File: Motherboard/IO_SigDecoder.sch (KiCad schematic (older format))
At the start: 8 parts, among them U30 74LS04, U34 74LS04, U35 74LS04, U36 74LS00, U37 74LS00, U38 74LS10

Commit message: Large sync
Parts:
- added R11: 6k2, Resistors_THT:R_Axial_DIN0204_L3.6mm_D1.6mm_P7.62mm_Horizontal, symbol Device:R
- added SW5: SW_DIP_x01, Housings_DIP:DIP-4_W7.62mm, symbol Switch:SW_DIP_x01
- added U50: 74LS04, Housings_DIP:DIP-14_W7.62mm_Socket, symbol 74xx:74LS04
- added U51: ATF750LVC, Housings_DIP:DIP-28_W7.62mm_Socket, symbol fdc:ATF750LVC
- added U52: 74LS74, Housings_DIP:DIP-14_W7.62mm_Socket, symbol 74xx:74LS74
- added U53: 74LS00, Housings_DIP:DIP-14_W7.62mm_Socket, symbol 74xx:74LS00
- added U54: 74LS08, Housings_DIP:DIP-14_W7.62mm_Socket, symbol 74xx:74LS08
- added U55: 74LS138, Housings_DIP:DIP-16_W7.62mm_Socket, symbol 74xx:74LS138
- added U56: 4077, Housings_DIP:DIP-14_W7.62mm_Socket, symbol 4xxx:4077
- added U57: DS1100Z-100+ (TTLDL-20), Housings_SOIC:SOIC-8_3.9x4.9mm_Pitch1.27mm, symbol DS1100Z-100+:DS1100Z-100+
- added U?: CD40147, MODULE, symbol CD40147:CD40147
- R10, R9: footprint (none) -> Resistors_THT:R_Axial_DIN0204_L3.6mm_D1.6mm_P7.62mm_Horizontal
- U30, U34, U35, U36, U37, U38: footprint (none) -> Housings_DIP:DIP-14_W7.62mm_Socket
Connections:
- net +5V: now also R11.2, U52.4 (~S), U55.16 (VCC)
- net at U38.12: now also U54.1
- new net: U53.3, U55.5 (E2)
- new net: R11.1, SW5.2, U53.2
- new net ALLOW_NMI: U52.5 (Q), U54.2
- new net GND: SW5.1, U55.8 (GND)
- new net NMI: U54.3
- new net RESET: U50.1
- new net ROMADDRSEL: U56.3
- new net XA15: U55.1 (A0)
- new net XA16: U55.2 (A1)
- new net XA17: U55.3 (A2)
- new net XA18: U53.1
- new net XA19: U55.6 (E3)
- new net XD7: U52.2 (D)
- new net ~CS6: U55.9 (O6), U56.1
- new net ~CS7: U55.7 (O7), U56.2
- new net ~RESET: U50.2, U52.1 (~R)
- new net ~WATNMIREG: U52.3 (C)
- new net ~XMEMR: U55.4 (E1)
- no-connect marks 0 -> 6
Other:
- note added: "Not used"
- note added: "U44 in techref"

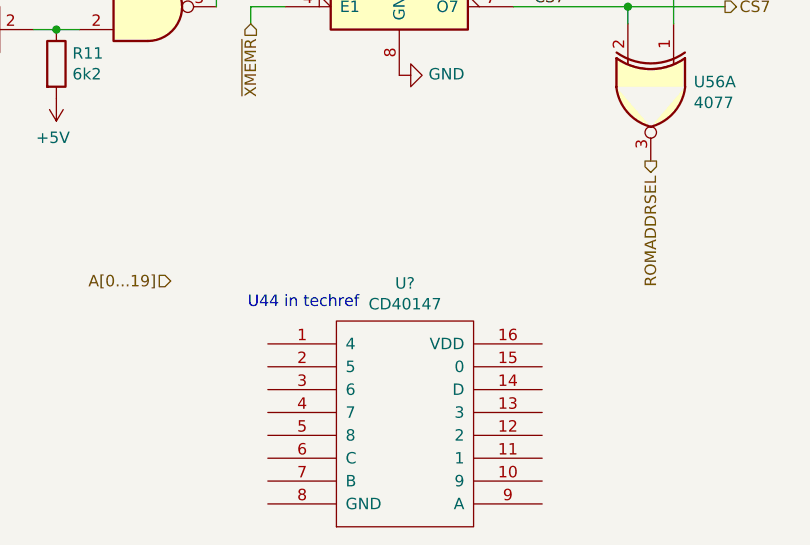
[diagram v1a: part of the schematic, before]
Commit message: Work on motherboard  - Integrating glue logic into CPLD  - Began work on routing
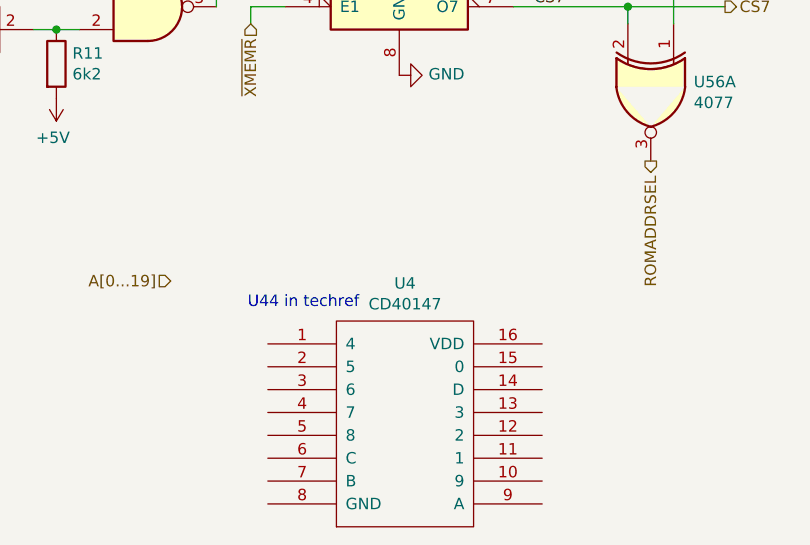
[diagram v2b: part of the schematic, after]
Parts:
- U4: renamed from U?; footprint MODULE -> Housings_DIP:DIP-16_W7.62mm_Socket
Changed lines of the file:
@@
 	1    0    0    -1
 $EndComp
-Wire Bus Line
-	6000 3725 6000 4125
 $Comp
-L CD40147:CD40147 U?
+L CD40147:CD40147 U4
 U 1 1 5CA70B41
 P 6775 6400
-F 0 "U?" H 6775 7015 50  0000 C CNN
+F 0 "U4" H 6775 7015 50  0000 C CNN
 F 1 "CD40147" H 6775 6924 50  0000 C CNN
-F 2 "MODULE" H 6775 6400 50  0001 C CNN
+F 2 "Housings_DIP:DIP-16_W7.62mm_Socket" H 6775 6400 50  0001 C CNN
 F 3 "DOCUMENTATION" H 6775 6400 50  0001 C CNN
 	1    6775 6400
@@
 Text Notes 6575 5900 2    50   ~ 0
 U44 in techref
+Wire Bus Line
+	6000 3725 6000 4125
 $EndSCHEMATC

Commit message: Large sync
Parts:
- removed R9: R, Resistors_THT:R_Axial_DIN0204_L3.6mm_D1.6mm_P7.62mm_Horizontal, symbol Device:R
- removed U35, U50: 74LS04, Housings_DIP:DIP-14_W7.62mm_Socket, symbol 74xx:74LS04
- removed unit 1 of U36
- removed unit 3 of U36
- removed U37, U53: 74LS00, Housings_DIP:DIP-14_W7.62mm_Socket, symbol 74xx:74LS00
- removed U38: 74LS10, Housings_DIP:DIP-14_W7.62mm_Socket, symbol 74xx:74LS10
- removed U52: 74LS74, Housings_DIP:DIP-14_W7.62mm_Socket, symbol 74xx:74LS74
- removed U54: 74LS08, Housings_DIP:DIP-14_W7.62mm_Socket, symbol 74xx:74LS08
- removed U55: 74LS138, Housings_DIP:DIP-16_W7.62mm_Socket, symbol 74xx:74LS138
- removed U56: 4077, Housings_DIP:DIP-14_W7.62mm_Socket, symbol 4xxx:4077
- added R9: 1k, symbol Device:R_Small
- U4: symbol CD40147:CD40147 -> Motherboard-rescue:CD40147-CD40147
- U51: symbol fdc:ATF750LVC -> Motherboard-rescue:ATF750LVC-fdc
- U57: symbol DS1100Z-100+:DS1100Z-100+ -> Motherboard-rescue:DS1100Z-100+-DS1100Z-100+
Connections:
- net +5V: now also U51.24 (VCC), R9.2
- net CLK: now also U30.3; no longer U34.1
- net CLK33: now also U34.1; no longer U30.3
- net GND: now also U51.12 (GND)
- net IOCHCK: now also U51.23 (I/O), U51.5 (IN), R9.1
- net N.P.INSTLSW: now also U51.3 (IN)
- net N.P.NPI: now also U51.2 (IN)
- net NMI: now also U51.22 (I/O)
- net RESET: now also U51.8 (IN)
- net ROMADDRSEL: now also U51.19 (I/O)
- net XA15: now also U51.18 (I/O)
- net XA16: now also U51.17 (I/O)
- net XA17: now also U51.16 (I/O)
- net XA18: now also U51.15 (I/O)
- net XA19: now also U51.14 (I/O)
- net XD7: now also U51.7 (IN)
- net ~CS6: now also U51.21 (I/O)
- net ~CS7: now also U51.20 (I/O)
- net ~ENABLEIOCK': now also U51.4 (IN)
- net ~PCK: now also U51.6 (IN)
- net ~XMEMR: now also U51.9 (I/O)
- net ~WRTNMIREG: now reaches U51.1 (CLK/IN)
- net at U51.11 (IN): now also R11.1, SW5.2
- no-connect marks 6 -> 0
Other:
- note removed: "Not used"
- moved on the sheet: R10, R11, SW5, U30B, U34A, U36B, U4, U51, U57
